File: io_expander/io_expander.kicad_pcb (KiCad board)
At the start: 2 copper layers, 54 x 29.2 mm, 40 parts, among them J1 LCSC C145956, J2 LCSC C145956, SW1 TS5220A, SW2 TS5220A, SW3 TS5220A, SW4 TS5220A, U1 TCA9534

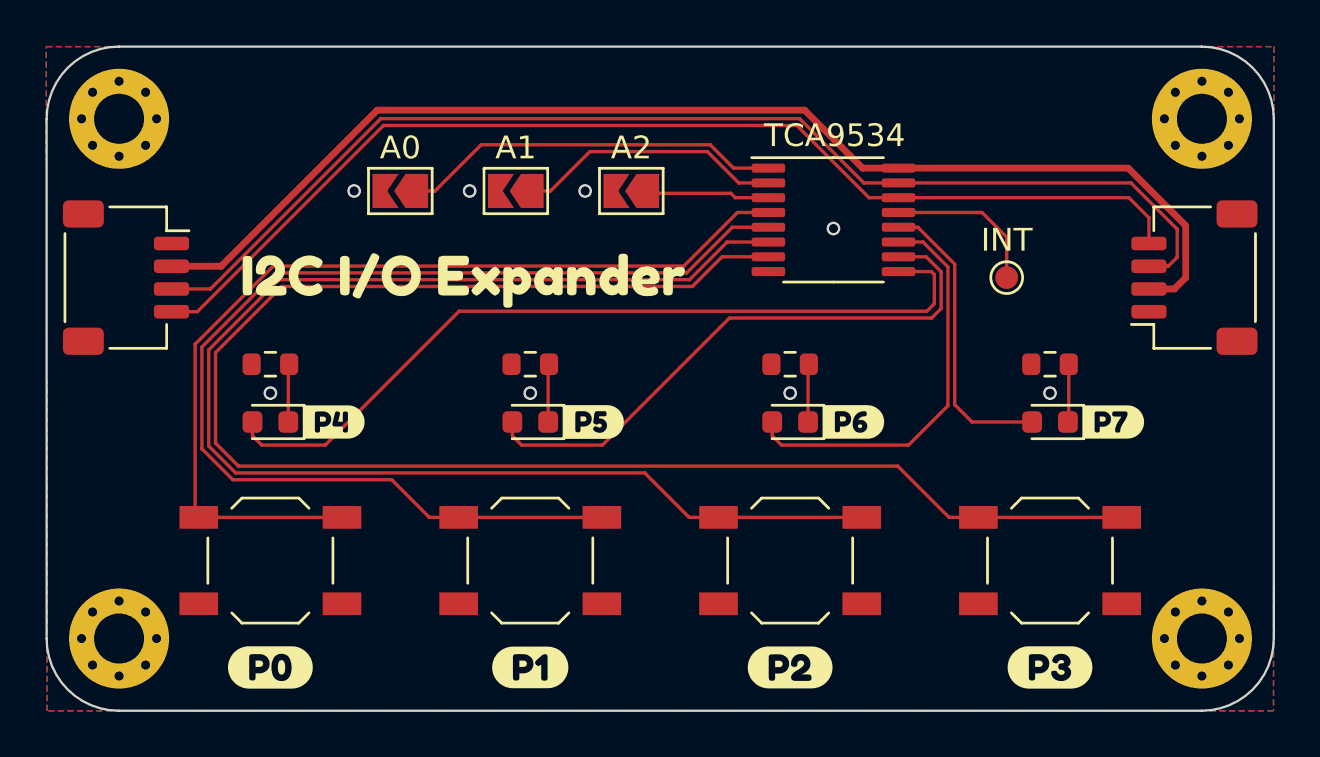
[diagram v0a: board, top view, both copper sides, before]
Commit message: Fixed I2C I/O Expander design
- Added pullup resistors on buttons
- Changed to 3 pin solder jumpers, to allow address pins to be tied to either VCC or GND
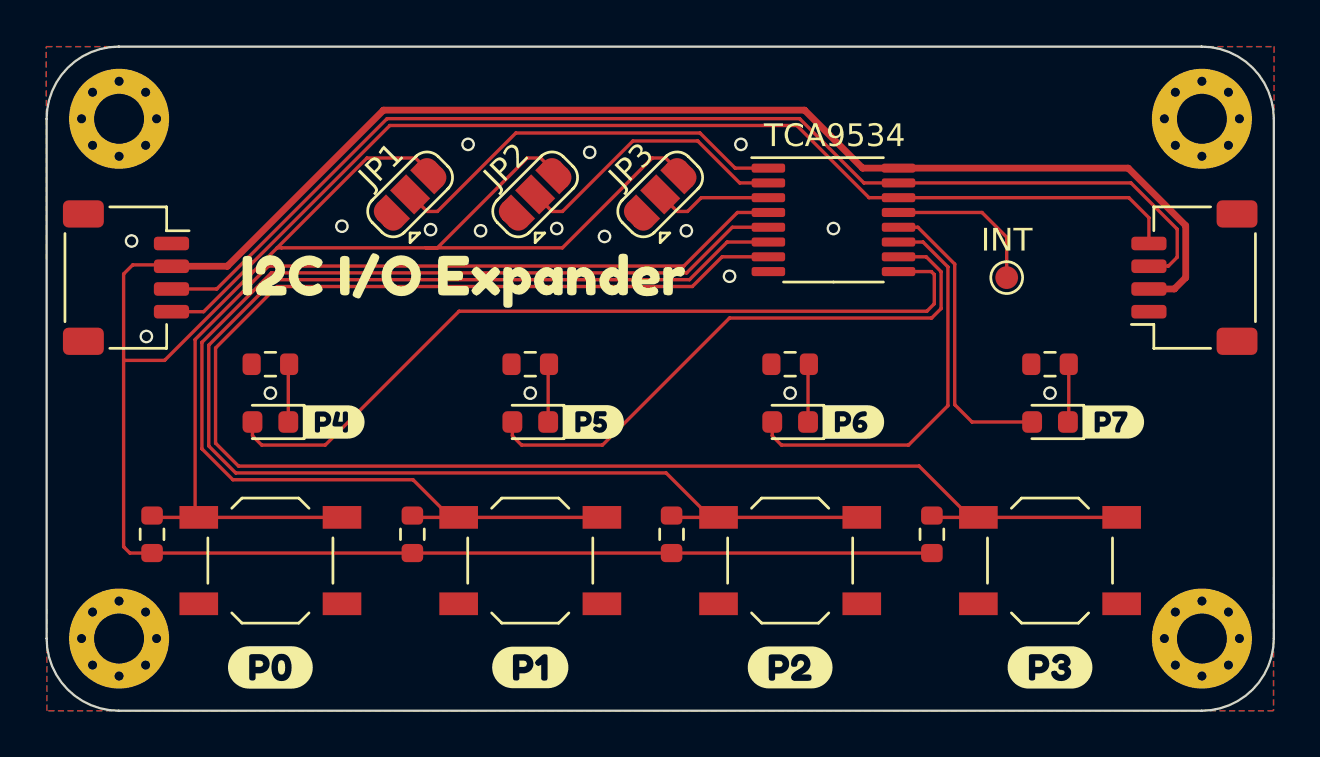
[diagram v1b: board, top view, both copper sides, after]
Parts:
- removed kibuzzard-6495A90E: G***, kibuzzard-6495A90E
- added R5: 10k, Resistor_SMD:R_0603_1608Metric, F.Cu at (68.1, 85.0)
- added R6: 10k, Resistor_SMD:R_0603_1608Metric, F.Cu at (79.6, 85.0)
- added R7: 10k, Resistor_SMD:R_0603_1608Metric, F.Cu at (91.0, 85.0)
- added R8: 10k, Resistor_SMD:R_0603_1608Metric, F.Cu at (102.4, 85.0)
- added kibuzzard-652C0514: G***, kibuzzard-652C0514, B.Cu at (108.3, 84.1)
- JP1: value A0 -> SolderJumper_3_Open; footprint Jumper:SolderJumper-2_P1.3mm_Open_TrianglePad1.0x1.5mm -> Jumper:SolderJumper-3_P1.3mm_Open_RoundedPad1.0x1.5mm
- JP2: value A1 -> SolderJumper_3_Open; footprint Jumper:SolderJumper-2_P1.3mm_Open_TrianglePad1.0x1.5mm -> Jumper:SolderJumper-3_P1.3mm_Open_RoundedPad1.0x1.5mm
- JP3: value A2 -> SolderJumper_3_Open; footprint Jumper:SolderJumper-2_P1.3mm_Open_TrianglePad1.0x1.5mm -> Jumper:SolderJumper-3_P1.3mm_Open_RoundedPad1.0x1.5mm
- moved JP3 1.28 mm to (90.5, 70.0), turned to 45 degrees
- moved JP2 0.86 mm to (85.0, 70.0), turned to 45 degrees
- moved JP1 0.46 mm to (79.5, 70.0), turned to 45 degrees
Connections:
- JP1 pad 1: Net-(JP1-A) -> GND
- JP1 pad 2: GND -> /A0
- JP2 pad 1: Net-(JP2-A) -> GND
- JP2 pad 2: GND -> /A1
- JP3 pad 1: Net-(JP3-A) -> GND
- JP3 pad 2: GND -> /A2
- U1 pad 1: Net-(JP1-A) -> /A0
- U1 pad 2: Net-(JP2-A) -> /A1
- U1 pad 3: Net-(JP3-A) -> /A2
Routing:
- net VCC: track 53.7 -> 148.4 mm
- net /A0: track 0.00 -> 18.1 mm
- net Net-(JP1-A): track 16.7 -> 0.00 mm
- net /A1: track 0.00 -> 12.6 mm
- net Net-(JP2-A): track 11.7 -> 0.00 mm
- net Net-(JP3-A): track 5.42 -> 0.00 mm
- net /A2: track 0.00 -> 5.32 mm
- net P2: track 60.8 -> 63.0 mm
- net P0: track 41.6 -> 43.8 mm
- net P3: track 71.2 -> 73.4 mm
- net P1: track 50.4 -> 52.6 mm
- net GND: vias 8 -> 17
